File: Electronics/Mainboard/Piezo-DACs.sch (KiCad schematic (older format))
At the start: 38 parts, among them U1 AD8676, U2 AD8676

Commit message: Mainboard layout and schematic done
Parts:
- C1, C2, C3, C4: LCSC (none) -> C14663
- C5, C6, C7, C8: LCSC (none) -> C15850
- C83, C84, C85, C86, C87, C88: value opt -> 220p; LCSC (none) -> C1603
- R1, R10, R11, R12, R13, R14, R2, R3, R4, R5, R6, R7, R8, R9: footprint Capacitor_SMD:C_0805_2012Metric_Pad1.15x1.40mm_HandSolder -> Resistor_SMD:R_0805_2012Metric; LCSC (none) -> C26010
- R15, R16, R17, R18: value 220 -> 49R9; footprint Capacitor_SMD:C_0805_2012Metric_Pad1.15x1.40mm_HandSolder -> Resistor_SMD:R_0805_2012Metric; LCSC (none) -> C17720
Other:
- note added: "DAC Outputs: +/- 10V"

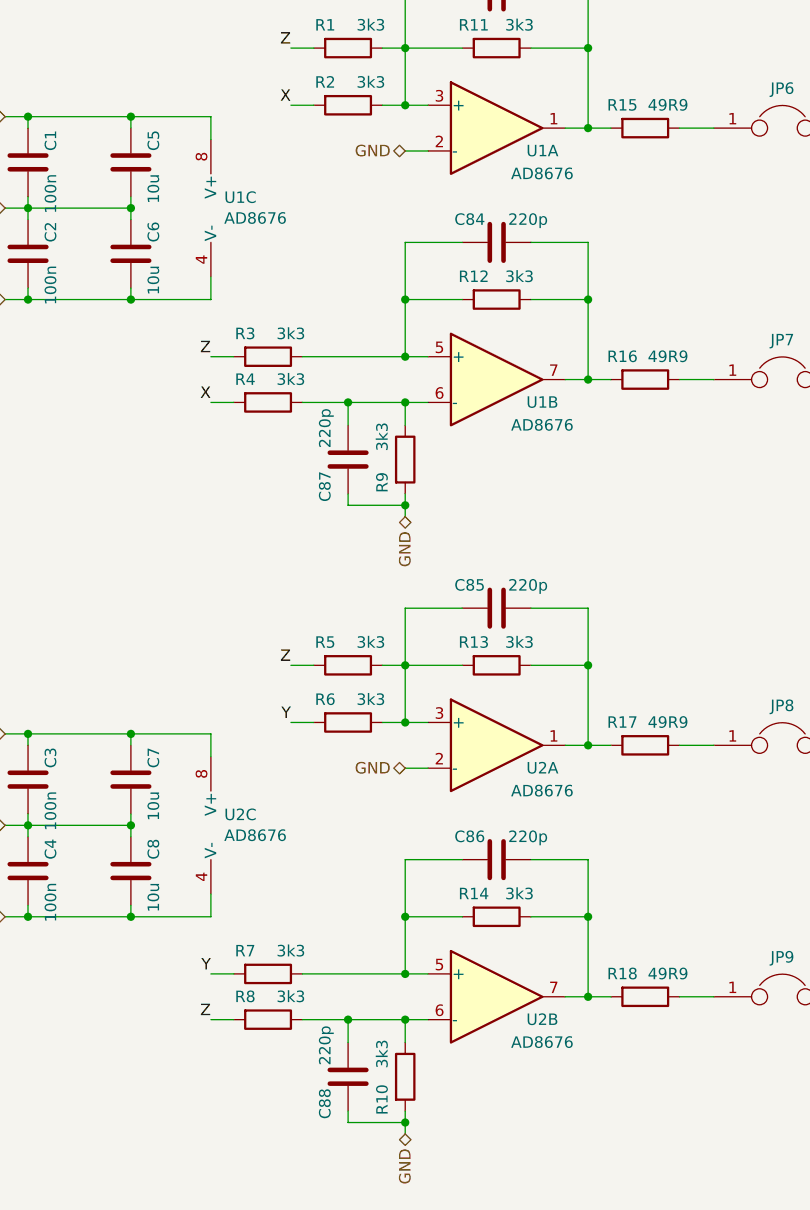
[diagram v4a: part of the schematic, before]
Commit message: Added images
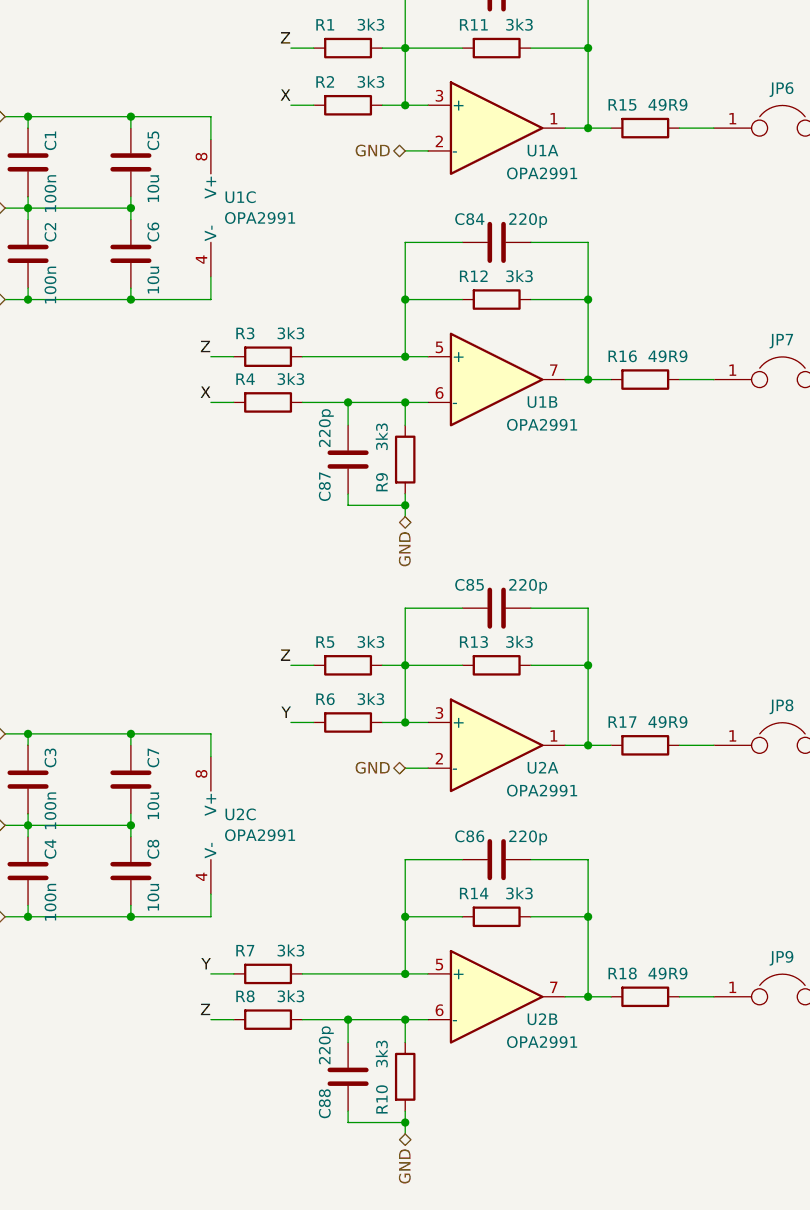
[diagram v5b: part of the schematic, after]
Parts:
- U1, U2: value AD8676 -> OPA2991; Digikey (none) -> 296-OPA2991IDRCT-ND
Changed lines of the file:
@@
 P 8650 1750
 F 0 "U1" H 8850 1650 50  0000 C CNN
-F 1 "AD8676" H 8850 1550 50  0000 C CNN
+F 1 "OPA2991" H 8850 1550 50  0000 C CNN
 F 2 "Package_SO:SOIC-8_3.9x4.9mm_P1.27mm" H 8650 1750 50  0001 C CNN
-F 3 "https://www.digikey.de/product-detail/de/analog-devices-inc/AD8676ARZ/AD8676ARZ-ND/1246063" H 8650 1750 50  0001 C CNN
+F 3 "https://www.ti.com/lit/ds/symlink/opa2991.pdf?ts=1594905249257&ref_url=https%253A%252F%252Fwww.ti.com%252Fproduct%252FOPA2991" H 8650 1750 50  0001 C CNN
 F 4 "" H 8650 1750 50  0001 C CNN "LCSC"
+F 5 "296-OPA2991IDRCT-ND " H 8650 1750 50  0001 C CNN "Digikey"
 	1    8650 1750
 	1    0    0    -1
@@
 P 8650 2850
 F 0 "U1" H 8850 2750 50  0000 C CNN
-F 1 "AD8676" H 8850 2650 50  0000 C CNN
+F 1 "OPA2991" H 8850 2650 50  0000 C CNN
 F 2 "Package_SO:SOIC-8_3.9x4.9mm_P1.27mm" H 8650 2850 50  0001 C CNN
-F 3 "https://www.digikey.de/product-detail/de/analog-devices-inc/AD8676ARZ/AD8676ARZ-ND/1246063" H 8650 2850 50  0001 C CNN
+F 3 "https://www.ti.com/lit/ds/symlink/opa2991.pdf?ts=1594905249257&ref_url=https%253A%252F%252Fwww.ti.com%252Fproduct%252FOPA2991" H 8650 2850 50  0001 C CNN
 F 4 "" H 8650 2850 50  0001 C CNN "LCSC"
+F 5 "296-OPA2991IDRCT-ND " H 8650 2850 50  0001 C CNN "Digikey"
 	2    8650 2850
 	1    0    0    -1
@@
 P 7500 2100
 F 0 "U1" H 7458 2146 50  0000 L CNN
-F 1 "AD8676" H 7458 2055 50  0000 L CNN
+F 1 "OPA2991" H 7458 2055 50  0000 L CNN
 F 2 "Package_SO:SOIC-8_3.9x4.9mm_P1.27mm" H 7500 2100 50  0001 C CNN
-F 3 "https://www.digikey.de/product-detail/de/analog-devices-inc/AD8676ARZ/AD8676ARZ-ND/1246063" H 7500 2100 50  0001 C CNN
+F 3 "https://www.ti.com/lit/ds/symlink/opa2991.pdf?ts=1594905249257&ref_url=https%253A%252F%252Fwww.ti.com%252Fproduct%252FOPA2991" H 7500 2100 50  0001 C CNN
 F 4 "" H 7500 2100 50  0001 C CNN "LCSC"
+F 5 "296-OPA2991IDRCT-ND " H 7500 2100 50  0001 C CNN "Digikey"
 	3    7500 2100
 	1    0    0    -1
@@
 P 8650 4450
 F 0 "U2" H 8850 4350 50  0000 C CNN
-F 1 "AD8676" H 8850 4250 50  0000 C CNN
+F 1 "OPA2991" H 8850 4250 50  0000 C CNN
 F 2 "Package_SO:SOIC-8_3.9x4.9mm_P1.27mm" H 8650 4450 50  0001 C CNN
-F 3 "https://www.digikey.de/product-detail/de/analog-devices-inc/AD8676ARZ/AD8676ARZ-ND/1246063" H 8650 4450 50  0001 C CNN
+F 3 "https://www.ti.com/lit/ds/symlink/opa2991.pdf?ts=1594905249257&ref_url=https%253A%252F%252Fwww.ti.com%252Fproduct%252FOPA2991" H 8650 4450 50  0001 C CNN
 F 4 "" H 8650 4450 50  0001 C CNN "LCSC"
+F 5 "296-OPA2991IDRCT-ND " H 8650 4450 50  0001 C CNN "Digikey"
 	1    8650 4450
 	1    0    0    -1
@@
 P 8650 5550
 F 0 "U2" H 8850 5450 50  0000 C CNN
-F 1 "AD8676" H 8850 5350 50  0000 C CNN
+F 1 "OPA2991" H 8850 5350 50  0000 C CNN
 F 2 "Package_SO:SOIC-8_3.9x4.9mm_P1.27mm" H 8650 5550 50  0001 C CNN
-F 3 "https://www.digikey.de/product-detail/de/analog-devices-inc/AD8676ARZ/AD8676ARZ-ND/1246063" H 8650 5550 50  0001 C CNN
+F 3 "https://www.ti.com/lit/ds/symlink/opa2991.pdf?ts=1594905249257&ref_url=https%253A%252F%252Fwww.ti.com%252Fproduct%252FOPA2991" H 8650 5550 50  0001 C CNN
 F 4 "" H 8650 5550 50  0001 C CNN "LCSC"
+F 5 "296-OPA2991IDRCT-ND " H 8650 5550 50  0001 C CNN "Digikey"
 	2    8650 5550
 	1    0    0    -1
@@
 P 7500 4800
 F 0 "U2" H 7458 4846 50  0000 L CNN
-F 1 "AD8676" H 7458 4755 50  0000 L CNN
+F 1 "OPA2991" H 7458 4755 50  0000 L CNN
 F 2 "Package_SO:SOIC-8_3.9x4.9mm_P1.27mm" H 7500 4800 50  0001 C CNN
-F 3 "https://www.digikey.de/product-detail/de/analog-devices-inc/AD8676ARZ/AD8676ARZ-ND/1246063" H 7500 4800 50  0001 C CNN
+F 3 "https://www.ti.com/lit/ds/symlink/opa2991.pdf?ts=1594905249257&ref_url=https%253A%252F%252Fwww.ti.com%252Fproduct%252FOPA2991" H 7500 4800 50  0001 C CNN
 F 4 "" H 7500 4800 50  0001 C CNN "LCSC"
+F 5 "296-OPA2991IDRCT-ND " H 7500 4800 50  0001 C CNN "Digikey"
 	3    7500 4800
 	1    0    0    -1

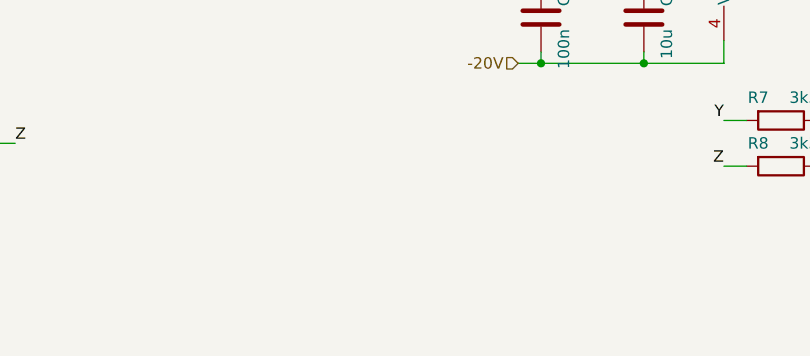
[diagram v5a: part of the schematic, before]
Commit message: Added sample-bias interconnect and base interconnect V2
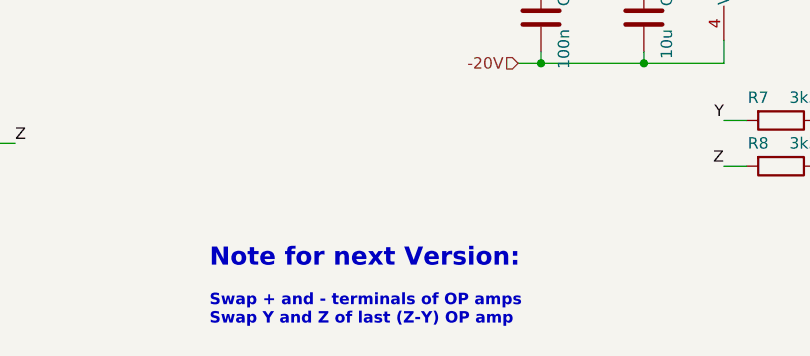
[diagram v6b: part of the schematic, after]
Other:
- note added: "Note for next Version:"
- note added: "Swap + and - terminals of OP amps\nSwap Y and Z of last (Z-Y) OP amp"
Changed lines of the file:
@@
 Text Notes 3100 1600 0    50   ~ 0
 DAC Outputs: +/- 10V
+Text Notes 5150 6100 0    79   ~ 16
+Note for next Version:
+Text Notes 5150 6350 0    50   ~ 10
+Swap + and - terminals of OP amps\nSwap Y and Z of last (Z-Y) OP amp
 $EndSCHEMATC

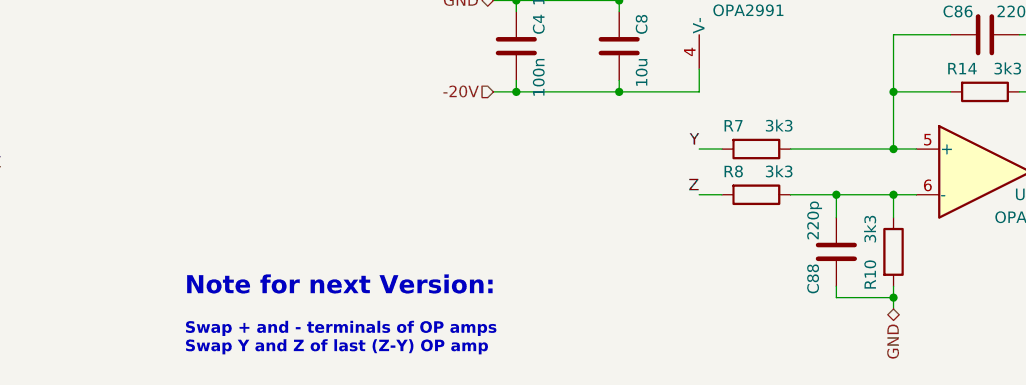
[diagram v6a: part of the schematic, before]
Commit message: Clearified warning in DAC op wiring
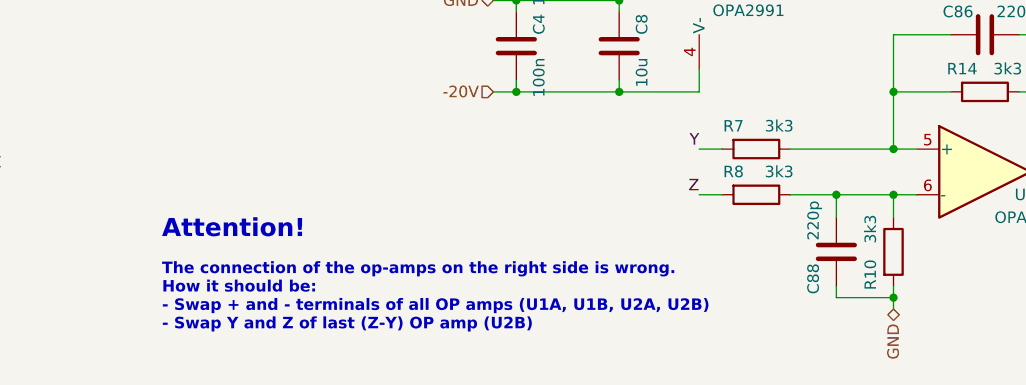
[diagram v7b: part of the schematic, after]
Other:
- note added: "Attention!"
- note added: "The connection of the op-amps on the right side is wrong.\nHow it should be:\n- Swap + and - terminals of all OP amps (U1A, U1B, U2A, U2B)\n- Swap Y and Z of last (Z-Y) OP amp (U2B)"
- note removed: "Note for next Version:"
- note removed: "Swap + and - terminals of OP amps\nSwap Y and Z of last (Z-Y) OP amp"
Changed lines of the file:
@@
 Text Notes 3100 1600 0    50   ~ 0
 DAC Outputs: +/- 10V
-Text Notes 5150 6100 0    79   ~ 16
-Note for next Version:
-Text Notes 5150 6350 0    50   ~ 10
-Swap + and - terminals of OP amps\nSwap Y and Z of last (Z-Y) OP amp
+Text Notes 5050 5850 0    79   ~ 16
+Attention!
+Text Notes 5050 6250 0    50   ~ 10
+The connection of the op-amps on the right side is wrong.\nHow it should be:\n- Swap + and - terminals of all OP amps (U1A, U1B, U2A, U2B)\n- Swap Y and Z of last (Z-Y) OP amp (U2B)
 $EndSCHEMATC
